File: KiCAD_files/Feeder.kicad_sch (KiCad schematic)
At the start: 64 parts, among them J301 Conn_01x03, Q301 60V N channel, Q302 TK13P25D,RQ, T301 PA2467NL, U301 NCP12700, U302 HMHA2801A, U303 HMHA2801A, U304 TL431MFDT,215, U305 TL431MFDT,215

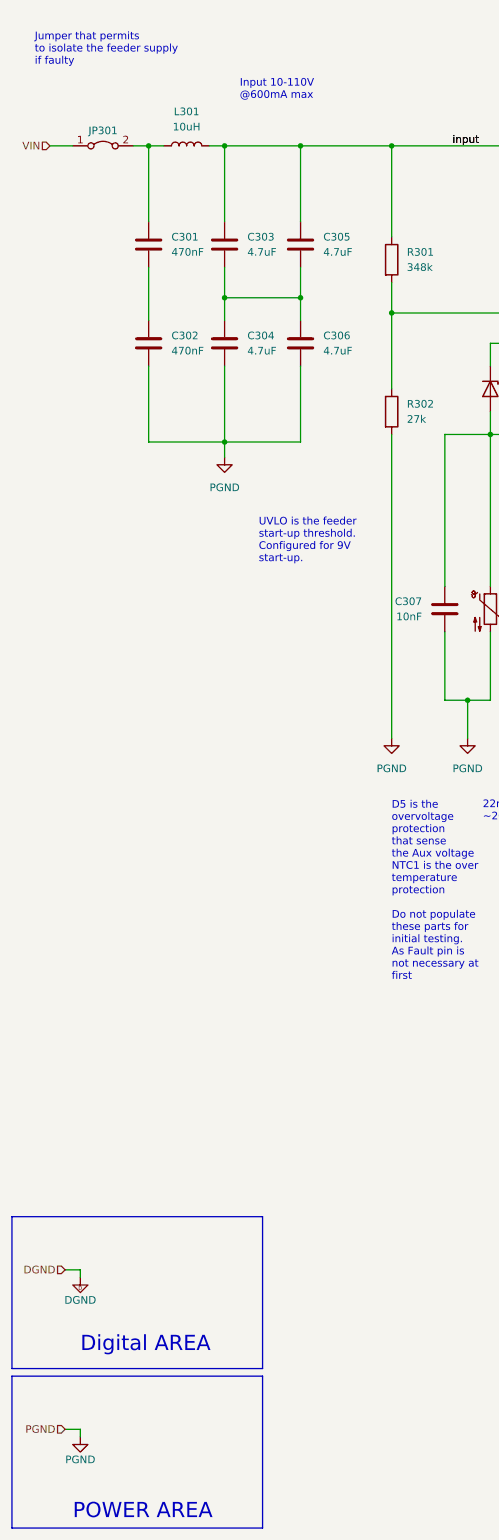
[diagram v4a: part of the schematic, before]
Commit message: removed power ports on hierarchical blocks
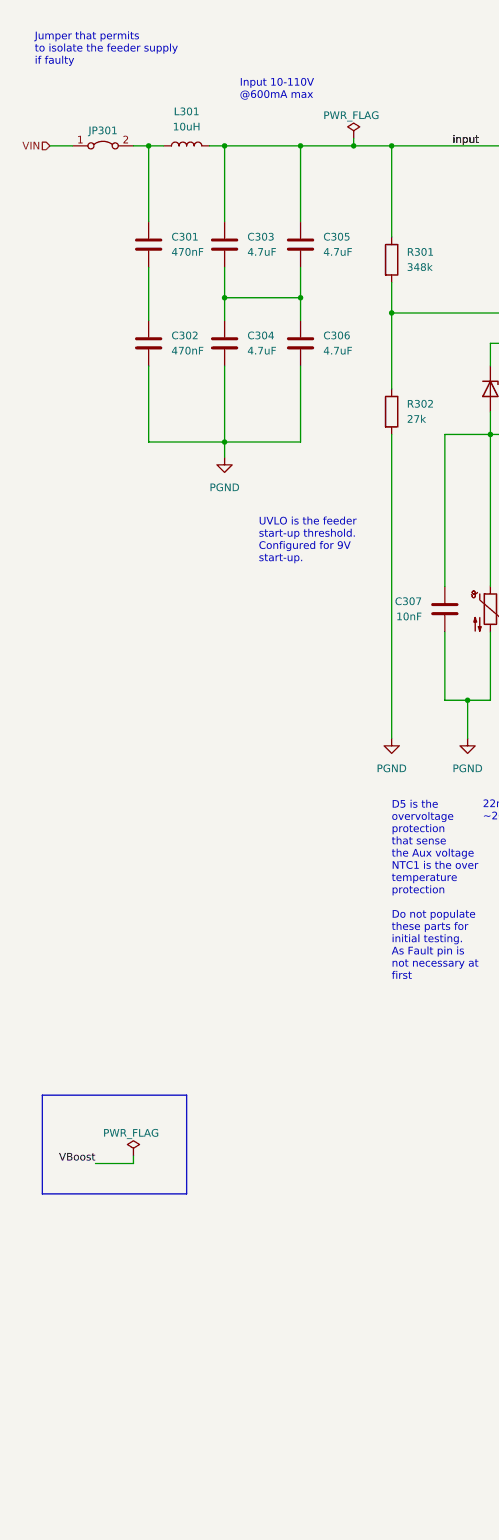
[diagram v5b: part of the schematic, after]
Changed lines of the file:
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@@
   (junction (at 265.43 105.41) (diameter 0) (color 0 0 0 0)
   )
+  (junction (at 71.12 46.99) (diameter 0) (color 0 0 0 0)
+  )
   (junction (at 205.74 83.82) (diameter 0) (color 0 0 0 0)
   )
@@
     (stroke (width 0) (type default))
   )
-  (wire (pts (xy 25.4 262.89) (xy 25.4 261.62))
-    (stroke (width 0) (type default))
-  )
   (wire (pts (xy 238.76 90.17) (xy 248.92 90.17))
     (stroke (width 0.5) (type default))
@@
     (stroke (width 0) (type default))
   )
+  (wire (pts (xy 71.12 46.99) (xy 71.12 45.72))
+    (stroke (width 0) (type default))
+  )
   (wire (pts (xy 215.9 87.63) (xy 215.9 83.82))
     (stroke (width 0) (type default))
   )
-  (wire (pts (xy 62.23 46.99) (xy 77.47 46.99))
+  (wire (pts (xy 62.23 46.99) (xy 71.12 46.99))
     (stroke (width 0.45) (type default))
   )
@@
     (stroke (width 0) (type default))
   )
+  (wire (pts (xy 71.12 46.99) (xy 77.47 46.99))
+    (stroke (width 0.45) (type default))
+  )
   (wire (pts (xy 177.8 140.97) (xy 177.8 152.4))
     (stroke (width 0) (type default))
@@
     (stroke (width 0) (type default))
   )
+  (wire (pts (xy 34.29 217.17) (xy 34.29 215.9))
+    (stroke (width 0) (type default))
+  )
   (wire (pts (xy 226.06 128.27) (xy 223.52 128.27))
     (stroke (width 0) (type default))
@@
     (stroke (width 0) (type default))
   )
+  (wire (pts (xy 27.94 217.17) (xy 34.29 217.17))
+    (stroke (width 0) (type default))
+  )
   (wire (pts (xy 62.23 83.82) (xy 62.23 96.52))
     (stroke (width 0.45) (type default))
@@
     (stroke (width 0) (type default))
   )
-  (wire (pts (xy 25.4 261.62) (xy 22.86 261.62))
-    (stroke (width 0) (type default))
-  )
   (wire (pts (xy 236.22 102.87) (xy 238.76 102.87))
     (stroke (width 0) (type default))
@@
     (stroke (width 0) (type default))
   )
-  (wire (pts (xy 25.4 234.95) (xy 22.86 234.95))
-    (stroke (width 0) (type default))
-  )
   (wire (pts (xy 185.42 135.89) (xy 200.66 135.89))
     (stroke (width 0) (type default))
@@
     (stroke (width 0.45) (type default))
   )
-  (wire (pts (xy 25.4 236.22) (xy 25.4 234.95))
-    (stroke (width 0) (type default))
-  )
   (wire (pts (xy 273.05 198.12) (xy 285.75 198.12))
     (stroke (width 0) (type default))
@@
     (stroke (width 0) (type default))
   )
-  (rectangle (start 13.97 226.06) (end 55.88 251.46)
-    (stroke (width 0) (type default))
-    (fill (type none))
-  )
-  (rectangle (start 13.97 252.73) (end 55.88 278.13)
+  (rectangle (start 19.05 205.74) (end 43.18 222.25)
     (stroke (width 0) (type default))
     (fill (type none))
@@
     (effects (font (size 1.27 1.27)) (justify left bottom))
   )
-  (text "POWER AREA\n" (at 24.13 276.86 0)
-    (effects (font (face "Arial") (size 2.54 2.54)) (justify left bottom))
-  )
   (text "Digital AREA\n" (at 234.95 17.78 0)
     (effects (font (size 2.54 2.54) (thickness 0.508) bold) (justify left bottom))
@@
     (effects (font (size 2.54 2.54) (thickness 0.508) bold) (justify left bottom))
   )
-  (text "Digital AREA\n" (at 25.4 248.92 0)
-    (effects (font (face "Arial") (size 2.54 2.54)) (justify left bottom))
-  )
   (text "22nF means \n~20ms soft start" (at 92.71 160.02 0)
     (effects (font (size 1.27 1.27)) (justify left bottom))
@@
     (effects (font (size 1.27 1.27)) (justify left bottom))
   )
+  (label "VBoost" (at 27.94 217.17 180) (fields_autoplaced)
+    (effects (font (size 1.27 1.27)) (justify right bottom))
+  )
   (label "VAUX" (at 100.33 80.01 180) (fields_autoplaced)
     (effects (font (size 1.27 1.27)) (justify right bottom))
@@
     (effects (font (size 1.27 1.27)) (justify left))
   )
-  (hierarchical_label "DGND" (shape input) (at 22.86 234.95 180) (fields_autoplaced)
-    (effects (font (size 1.27 1.27)) (justify right))
-  )
-  (hierarchical_label "PGND" (shape input) (at 22.86 261.62 180) (fields_autoplaced)
-    (effects (font (size 1.27 1.27)) (justify right))
-  )
   (symbol (lib_id "Device:Thermistor_NTC") (at 93.98 124.46 0) (unit 1)
     (in_bom yes) (on_board yes) (dnp no) (fields_autoplaced)
@@
     )
   )
-  (symbol (lib_id "power:GND") (at 25.4 262.89 0) (unit 1)
-    (in_bom yes) (on_board yes) (dnp no)
-    (property "Reference" "#PWR0103" (at 25.4 269.24 0)
-      (effects (font (size 1.27 1.27)) hide)
-    )
-    (property "Value" "PGND" (at 25.4 266.7 0)
-      (effects (font (size 1.27 1.27)))
-    )
-    (property "Footprint" "" (at 25.4 262.89 0)
-      (effects (font (size 1.27 1.27)) hide)
-    )
-    (property "Datasheet" "" (at 25.4 262.89 0)
-      (effects (font (size 1.27 1.27)) hide)
-    )
-    (pin "1")
-    (instances
-      (project "inverter"
-        (path "/8d0c1d66-35ef-4a53-a28f-436a11b54f42"
-          (reference "#PWR0103") (unit 1)
-        )
-        (path "/8d0c1d66-35ef-4a53-a28f-436a11b54f42/d5d50263-0660-44c8-a20f-043dc430c72e"
-          (reference "#PWR0571") (unit 1)
-        )
-        (path "/8d0c1d66-35ef-4a53-a28f-436a11b54f42/bce1534c-362e-45ed-a9dd-a44d6954485a"
-          (reference "#PWR0805") (unit 1)
-        )
-      )
-    )
-  )
   (symbol (lib_id "Device:C") (at 231.14 24.13 90) (unit 1)
     (in_bom yes) (on_board yes) (dnp no)
@@
       (effects (font (size 1.27 1.27)) hide)
     )
+    (property "Sim.Device" "D" (at 175.26 82.55 0)
+      (effects (font (size 1.27 1.27)) hide)
+    )
+    (property "Sim.Pins" "1=K 2=A" (at 175.26 82.55 0)
+      (effects (font (size 1.27 1.27)) hide)
+    )
     (pin "1")
     (pin "2")
@@
       (effects (font (size 1.27 1.27)) hide)
     )
+    (property "Sim.Device" "D" (at 170.18 125.73 0)
+      (effects (font (size 1.27 1.27)) hide)
+    )
+    (property "Sim.Pins" "1=K 2=A" (at 170.18 125.73 0)
+      (effects (font (size 1.27 1.27)) hide)
+    )
     (pin "1")
     (pin "2")
@@
     )
   )
+  (symbol (lib_id "power:PWR_FLAG") (at 71.12 45.72 0) (unit 1)
+    (in_bom yes) (on_board yes) (dnp no)
+    (property "Reference" "#FLG0101" (at 71.12 43.815 0)
+      (effects (font (size 1.27 1.27)) hide)
+    )
+    (property "Value" "PWR_FLAG" (at 66.04 41.91 0)
+      (effects (font (size 1.27 1.27)) (justify left))
+    )
+    (property "Footprint" "" (at 71.12 45.72 0)
+      (effects (font (size 1.27 1.27)) hide)
+    )
+    (property "Datasheet" "~" (at 71.12 45.72 0)
+      (effects (font (size 1.27 1.27)) hide)
+    )
+    (pin "1")
+    (instances
+      (project "inverter"
+        (path "/8d0c1d66-35ef-4a53-a28f-436a11b54f42"
+          (reference "#FLG0101") (unit 1)
+        )
+        (path "/8d0c1d66-35ef-4a53-a28f-436a11b54f42/bce1534c-362e-45ed-a9dd-a44d6954485a"
+          (reference "#FLG0102") (unit 1)
+        )
+      )
+    )
+  )
   (symbol (lib_id "power:GND") (at 189.23 152.4 0) (unit 1)
     (in_bom yes) (on_board yes) (dnp no)
@@
     )
   )
+  (symbol (lib_id "power:PWR_FLAG") (at 34.29 215.9 0) (unit 1)
+    (in_bom yes) (on_board yes) (dnp no)
+    (property "Reference" "#FLG0101" (at 34.29 213.995 0)
+      (effects (font (size 1.27 1.27)) hide)
+    )
+    (property "Value" "PWR_FLAG" (at 29.21 212.09 0)
+      (effects (font (size 1.27 1.27)) (justify left))
+    )
+    (property "Footprint" "" (at 34.29 215.9 0)
+      (effects (font (size 1.27 1.27)) hide)
+    )
+    (property "Datasheet" "~" (at 34.29 215.9 0)
+      (effects (font (size 1.27 1.27)) hide)
+    )
+    (pin "1")
+    (instances
+      (project "inverter"
+        (path "/8d0c1d66-35ef-4a53-a28f-436a11b54f42"
+          (reference "#FLG0101") (unit 1)
+        )
+        (path "/8d0c1d66-35ef-4a53-a28f-436a11b54f42/bce1534c-362e-45ed-a9dd-a44d6954485a"
+          (reference "#FLG0103") (unit 1)
+        )
+      )
+    )
+  )
   (symbol (lib_id "Device:C") (at 165.1 68.58 0) (unit 1)
     (in_bom yes) (on_board yes) (dnp no)
@@
         )
       )
-    )
-  )
-  (symbol (lib_id "Symbols:DGND") (at 25.4 236.22 0) (unit 1)
-    (in_bom yes) (on_board yes) (dnp no)
-    (property "Reference" "#PWR0113" (at 25.4 242.57 0)
-      (effects (font (size 1.27 1.27)) hide)
-    )
-    (property "Value" "DGND" (at 25.4 240.03 0)
-      (effects (font (size 1.27 1.27)))
-    )
-    (property "Footprint" "" (at 25.4 236.22 0)
-      (effects (font (size 1.27 1.27)) hide)
-    )
-    (property "Datasheet" "" (at 25.4 236.22 0)
-      (effects (font (size 1.27 1.27)) hide)
-    )
-    (pin "1")
-    (instances
-      (project "inverter"
-        (path "/8d0c1d66-35ef-4a53-a28f-436a11b54f42"
-          (reference "#PWR0113") (unit 1)
-        )
-        (path "/8d0c1d66-35ef-4a53-a28f-436a11b54f42/d5d50263-0660-44c8-a20f-043dc430c72e"
-          (reference "#PWR0567") (unit 1)
-        )
-        (path "/8d0c1d66-35ef-4a53-a28f-436a11b54f42/bce1534c-362e-45ed-a9dd-a44d6954485a"
-          (reference "#PWR0804") (unit 1)
-        )
-      )
